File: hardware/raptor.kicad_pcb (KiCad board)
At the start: 4 copper layers, 22.9 x 57.7 mm, 70 parts, among them IC1 RAPTORQFN56, IC2 FT232H, IC3 MCP1755, IC4 93C56, IC5 TMUX1574RSVR, J1 USB, J11 CONN_20, J12 CONN_20, J2 Conn_01x02_Male, J3 Conn_01x02_Male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

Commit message: adjusted logo on silkscreen
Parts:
- moved D4 7.95 mm to (142.1, 94.6), turned to 270 degrees
- moved G1 3.79 mm to (145.9, 98.5)
- moved R9 1.37 mm to (151.7, 98.5), turned to 90 degrees
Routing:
- net GND: track 245.7 -> 243.3 mm
- net /MEM_SCK: track 29.8 -> 31.8 mm
- net Net-(IC2-Pad5): track 9.35 -> 11.2 mm
- net Net-(D4-Pad2): track 5.70 -> 6.72 mm
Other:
- board text added: "PWR"
- board text added: "Rev B"
- board text added: "reset"

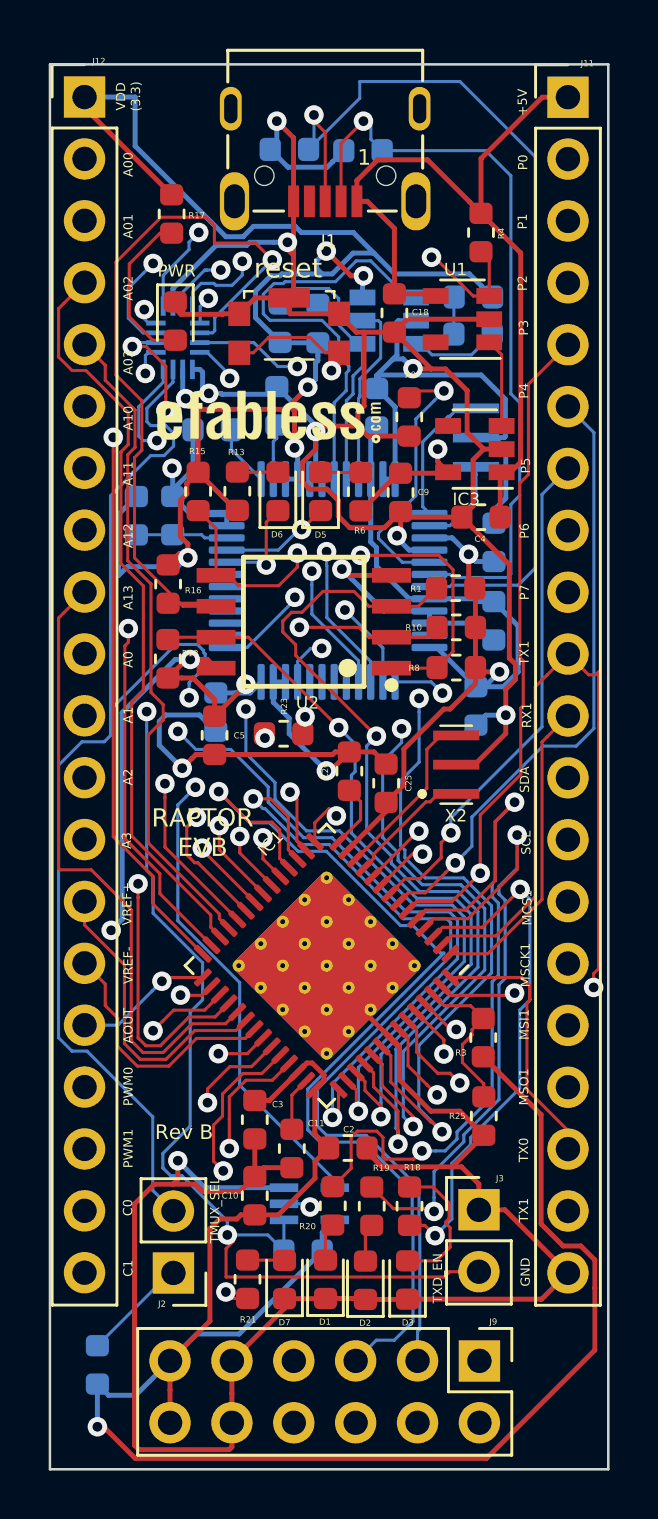
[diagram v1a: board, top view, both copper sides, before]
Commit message: Revert "adjusted logo on silkscreen"
This reverts commit 2ac67c38
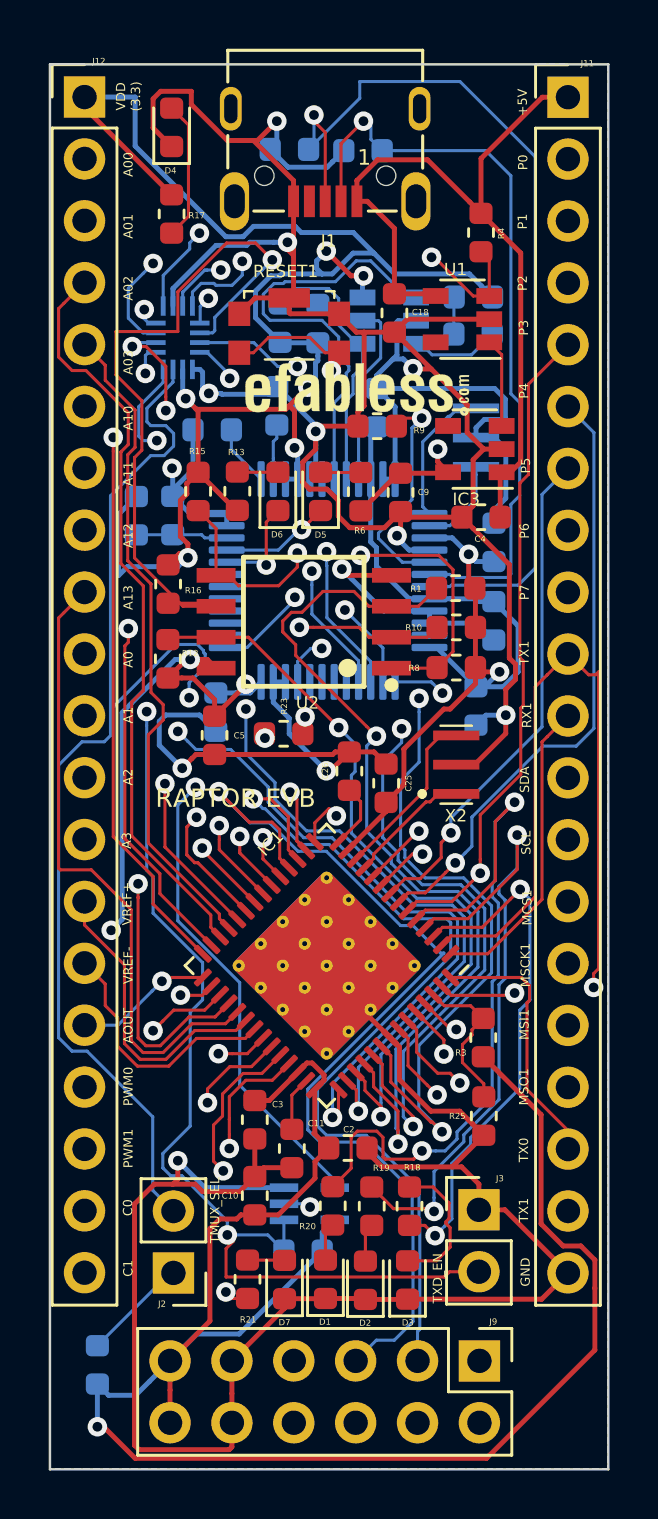
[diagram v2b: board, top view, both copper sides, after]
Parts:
- moved D4 7.95 mm to (142.0, 86.6), turned to 90 degrees
- moved G1 3.79 mm to (149.5, 97.4)
- moved R9 1.37 mm to (150.4, 98.9), turned to 0 degrees
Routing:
- net GND: track 243.3 -> 245.7 mm
- net /MEM_SCK: track 31.8 -> 29.8 mm
- net Net-(IC2-Pad5): track 11.2 -> 9.35 mm
- net Net-(D4-Pad2): track 6.72 -> 5.70 mm
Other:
- board text removed: "PWR"
- board text removed: "Rev B"
- board text removed: "reset"
